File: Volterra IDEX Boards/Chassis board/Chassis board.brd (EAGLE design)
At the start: 102.2 x 54 mm, 28 parts, among them K1 FFC/FPC/34PIN/1MMPITCH/TOPLOCK, K2 FFC/FPC/34PIN/1MMPITCH/TOPLOCK, K3 FFC/FPC/34PIN/1MMPITCH/TOPLOCK

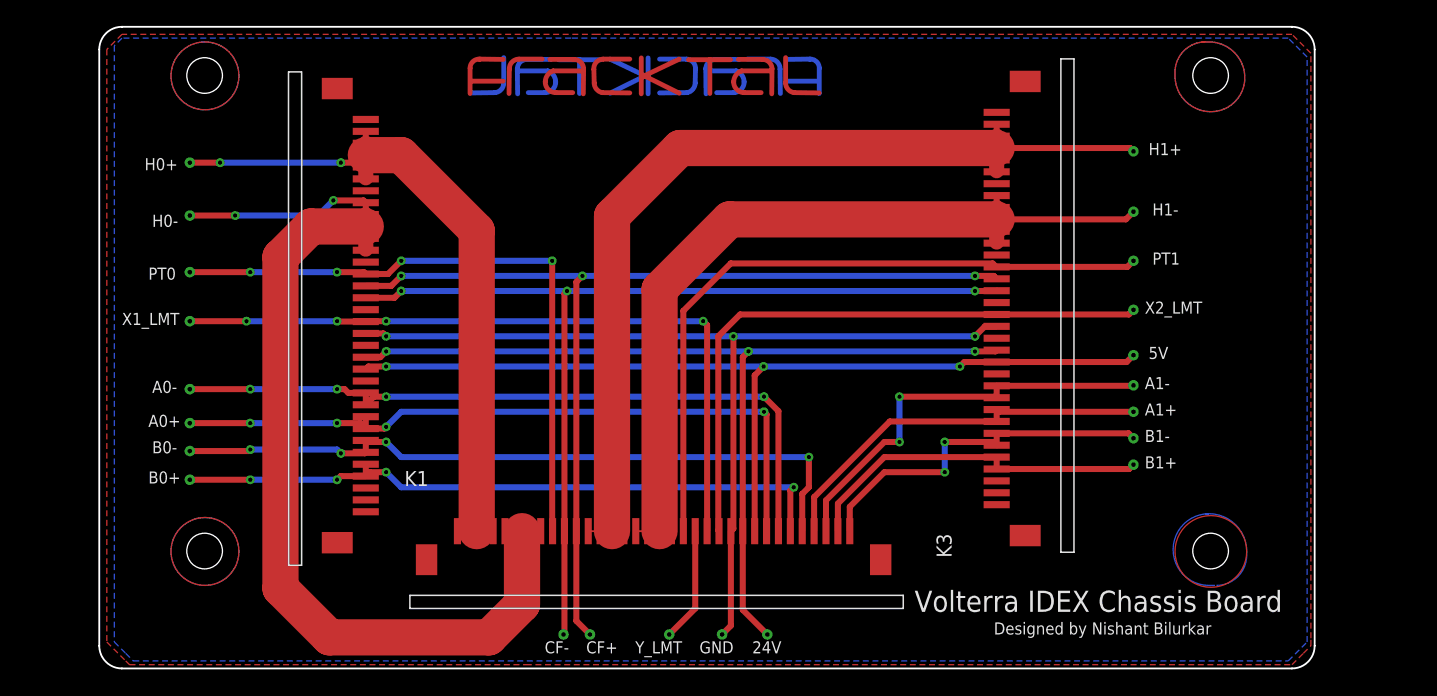
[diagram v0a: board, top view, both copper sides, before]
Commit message: Switching of carriage board numbering, changing extruder FFC pins and fixing routings
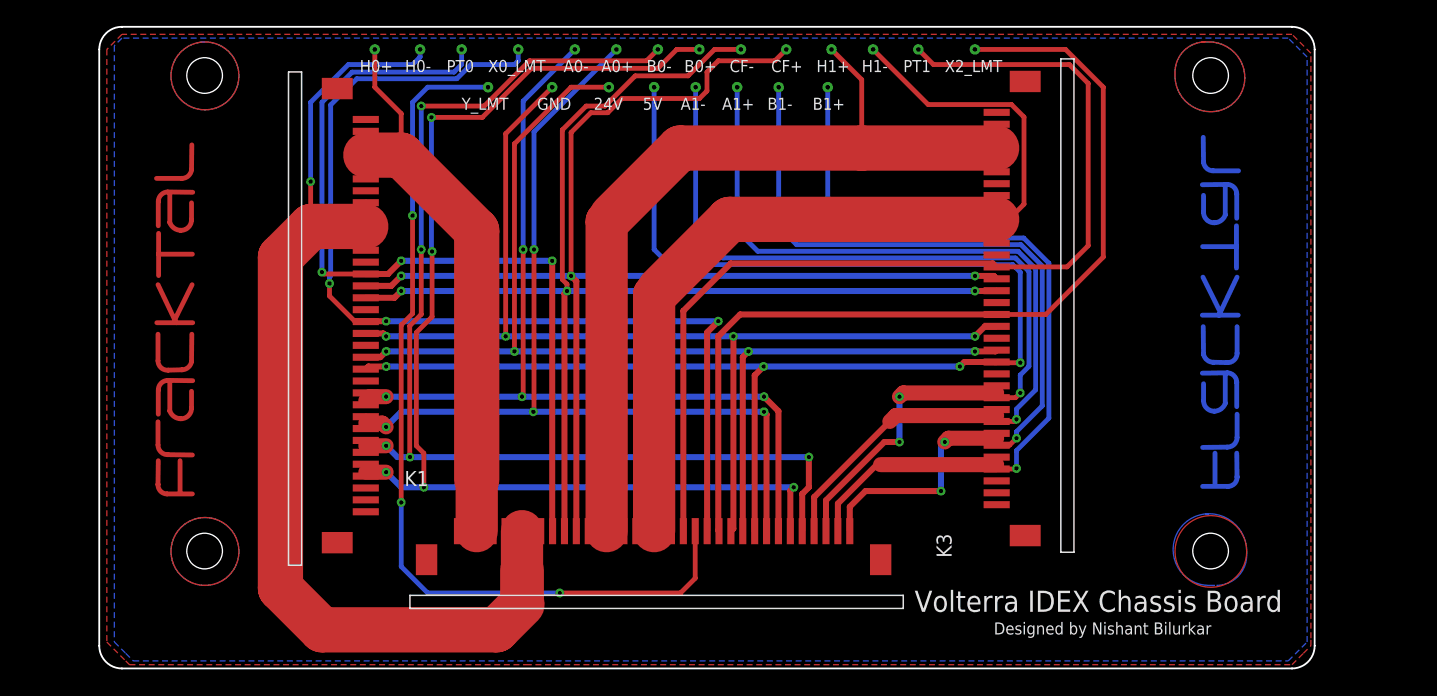
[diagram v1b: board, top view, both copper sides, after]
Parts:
- moved TP19 56.1 mm to (58.1, 55.9)
- moved TP3 51.9 mm to (65.4, 55.9)
- moved TP18 51.9 mm to (54.6, 55.9)
- moved TP4 51.4 mm to (61.6, 55.9)
- moved U$3 48.9 mm to (100.3, 31.1), turned to 90 degrees
- moved TP13 48.5 mm to (40.3, 52.7)
- moved TP6 48.2 mm to (45.7, 52.7)
- moved TP7 47.9 mm to (50.5, 52.7)
- moved TP20 47.7 mm to (51.1, 55.9)
- moved TP8 46.2 mm to (54.3, 52.7)
- moved TP14 44.6 mm to (57.8, 52.7)
- moved TP9 43.2 mm to (47.6, 55.9)
- moved TP15 43.1 mm to (61.3, 52.7)
- moved TP16 42.0 mm to (64.8, 52.7)
- moved U$2 41.3 mm to (15.6, 30.5), turned to 90 degrees
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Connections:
- removed net X2_LMT: K1.23, K3.17, TP12.P$1
- new net X0_LMT: K1.22, K2.18, TP5.P$1
- net X1_LMT: now also K1.23, K3.17, TP12.P$1; no longer K1.22, K2.18, TP5.P$1
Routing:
- net X0_LMT: track 0.00 -> 86.1 mm, vias 0 -> 3
- net Y_LMT: track 9.60 -> 76.4 mm, vias 0 -> 3
- net X2_LMT: track 52.3 -> 0.00 mm
- net 5V: track 79.2 -> 122.6 mm, vias 3 -> 4
- net A1-: track 35.4 -> 78.1 mm, vias 2 -> 3
- net A1+: track 33.4 -> 75.6 mm, vias 0 -> 1
- net B0+: track 56.4 -> 98.2 mm, vias 4 -> 5
- net B1-: track 30.9 -> 72.6 mm, vias 2 -> 3
- net B1+: track 30.0 -> 69.4 mm, vias 0 -> 1
- net B0-: track 60.4 -> 96.9 mm, vias 4 -> 5
- net PT1: track 58.4 -> 84.3 mm
- net CF+: track 84.4 -> 109.2 mm
- net CF-: track 82.3 -> 105.1 mm
- net A0+: track 60.2 -> 78.7 mm
- net 24V: track 78.2 -> 96.0 mm, vias 3 -> 4
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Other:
- board text added: "X0_LMT"
- board text removed: "X1_LMT"

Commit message: Updated Daughter board schematic and other boards
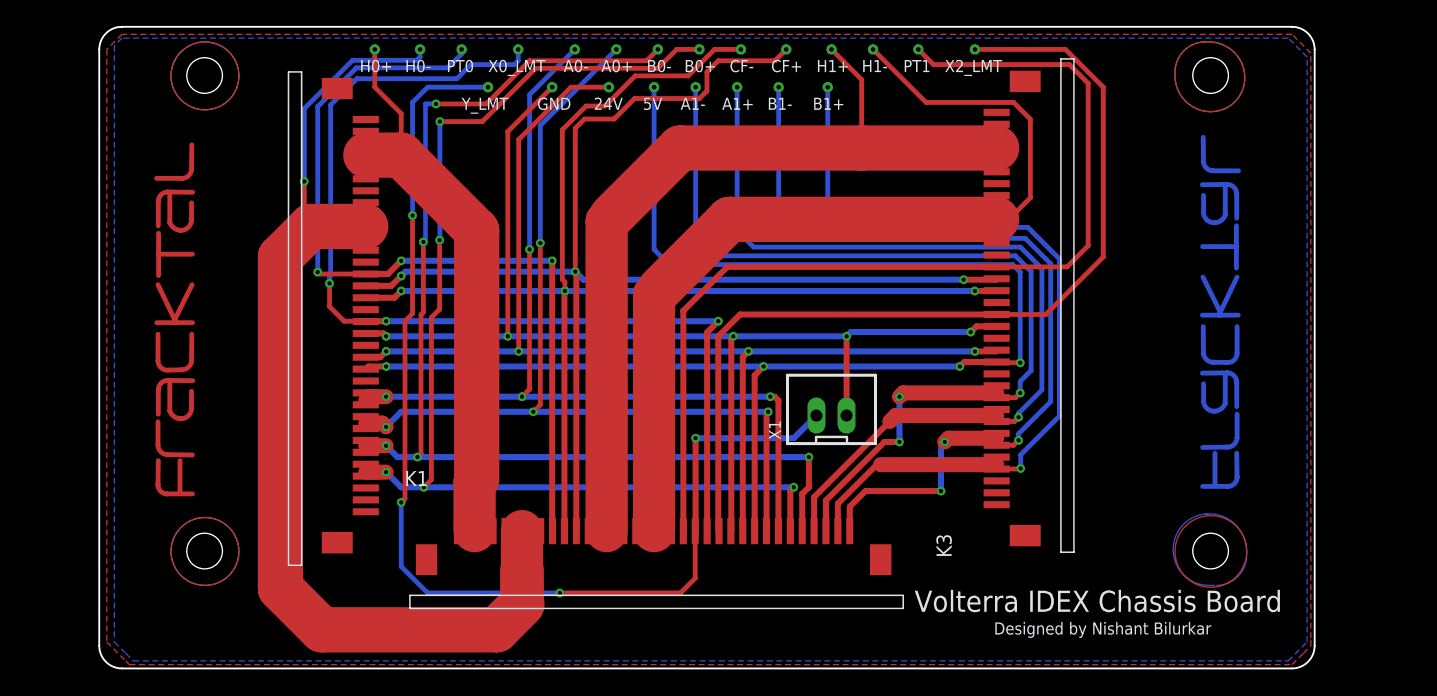
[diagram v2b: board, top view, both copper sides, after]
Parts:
- added X1: JST-XH-02-PIN-LONG-PAD, Rembrandt Electronics - JST XH Connectors v1-0:JST-XH-02-PACKAGE-LONG-PAD
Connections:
- net GND: now also X1.2
- net Y_LMT: now also X1.1
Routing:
- net Y_LMT: track 76.4 -> 95.7 mm, vias 3 -> 4
- net GND: track 92.6 -> 99.2 mm, vias 4 -> 5
- net B1+: track 69.4 -> 71.0 mm
- net B1-: track 72.6 -> 73.9 mm
- net B0+: track 98.2 -> 97.0 mm
- net A1+: track 75.6 -> 76.4 mm
- net H1-: track 83.5 -> 84.2 mm
- net X0_LMT: track 86.1 -> 86.6 mm
- net A0-: track 77.5 -> 78.0 mm

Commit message: DRC checked of Chassis, Carriage 1 & 2, and created CAM files
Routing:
- net H0+: track 53.9 -> 55.4 mm
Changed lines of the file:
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@@
 <contactref element="K2" pad="6"/>
 <contactref element="TP21" pad="P$1"/>
-<wire x1="37.7505" y1="15.3595" x2="38.7505" y2="15.3595" width="0.1524" layer="1"/>
-<wire x1="38.7505" y1="15.3595" x2="39.1922" y2="15.3595" width="0.1524" layer="1"/>
-<wire x1="39.37" y1="15.3595" x2="39.7505" y2="15.3595" width="0.1524" layer="1"/>
-<wire x1="39.7505" y1="15.3595" x2="40.7505" y2="15.3595" width="0.1524" layer="1"/>
-<wire x1="39.1922" y1="19.5072" x2="39.37" y2="19.685" width="3.556" layer="1"/>
-<wire x1="39.1922" y1="19.5072" x2="39.1922" y2="15.3595" width="3.556" layer="1"/>
-<wire x1="39.37" y1="19.685" x2="39.37" y2="40.64" width="3.81" layer="1"/>
+<wire x1="39.1922" y1="18.796" x2="39.37" y2="18.9738" width="3.556" layer="1"/>
+<wire x1="39.1922" y1="15.7151" x2="39.1922" y2="18.796" width="3.556" layer="1"/>
+<wire x1="39.37" y1="18.9738" x2="39.37" y2="40.64" width="3.81" layer="1"/>
 <wire x1="30.04" y1="46.99" x2="33.02" y2="46.99" width="3.81" layer="1"/>
 <wire x1="39.37" y1="40.64" x2="33.02" y2="46.99" width="3.81" layer="1"/>
@@
 <wire x1="30.04" y1="46.99" x2="30.04" y2="45.99" width="0.508" layer="1"/>
 <wire x1="30.04" y1="45.99" x2="30.04" y2="44.99" width="0.508" layer="1"/>
+<wire x1="40.7505" y1="15.3595" x2="39.7505" y2="15.3595" width="0.2032" layer="1"/>
+<wire x1="37.7505" y1="15.3595" x2="38.7505" y2="15.3595" width="0.2032" layer="1"/>
+<wire x1="38.7505" y1="15.3595" x2="39.7505" y2="15.3595" width="0.2032" layer="1"/>
+<wire x1="37.7505" y1="15.3595" x2="38.1061" y2="15.7151" width="0.2032" layer="1"/>
+<wire x1="38.1061" y1="15.7151" x2="39.1922" y2="15.7151" width="0.2032" layer="1"/>
 </signal>
 <signal name="H0-">
@@
 <contactref element="K2" pad="11"/>
 <contactref element="TP1" pad="P$1"/>
-<wire x1="41.7505" y1="15.3595" x2="42.7505" y2="15.3595" width="0.1524" layer="1"/>
-<wire x1="43.7505" y1="15.3595" x2="43.18" y2="15.3595" width="0.1524" layer="1"/>
-<wire x1="42.7505" y1="15.3595" x2="43.18" y2="15.3595" width="0.1524" layer="1"/>
-<wire x1="43.7505" y1="15.3595" x2="44.7505" y2="15.3595" width="0.1524" layer="1"/>
-<wire x1="43.18" y1="15.3595" x2="43.18" y2="12.065" width="3.556" layer="1"/>
+<wire x1="43.18" y1="12.065" x2="43.18" y2="15.1817" width="3.556" layer="1"/>
 <wire x1="43.18" y1="12.065" x2="43.18" y2="9.2075" width="3.683" layer="1"/>
 <wire x1="43.18" y1="9.2075" x2="41.0337" y2="7.0612" width="3.81" layer="1"/>
@@
 <wire x1="30.04" y1="40.99" x2="30.04" y2="39.99" width="1.27" layer="1"/>
 <wire x1="30.04" y1="41.99" x2="30.04" y2="42.99" width="0.508" layer="1"/>
-<wire x1="30.04" y1="39.99" x2="30.04" y2="38.99" width="0.1524" layer="1"/>
 <wire x1="25.4325" y1="40.99" x2="24.8666" y2="41.5559" width="0.4064" layer="1"/>
 <wire x1="24.8666" y1="41.5559" x2="24.8666" y2="44.7675" width="0.4064" layer="1"/>
@@
 <wire x1="34.3281" y1="54.9656" x2="34.6075" y2="55.245" width="0.4064" layer="16"/>
 <wire x1="34.6075" y1="55.245" x2="34.6075" y2="55.88" width="0.4064" layer="16"/>
+<wire x1="41.7505" y1="15.3595" x2="42.7505" y2="15.3595" width="0.2032" layer="1"/>
+<wire x1="42.7505" y1="15.3595" x2="43.7505" y2="15.3595" width="0.2032" layer="1"/>
+<wire x1="43.7505" y1="15.3595" x2="44.7505" y2="15.3595" width="0.2032" layer="1"/>
+<wire x1="43.18" y1="15.1817" x2="43.3578" y2="15.3595" width="0.2032" layer="1"/>
+<wire x1="43.3578" y1="15.3595" x2="43.7505" y2="15.3595" width="0.2032" layer="1"/>
+<wire x1="30.04" y1="39.99" x2="30.04" y2="38.99" width="0.2032" layer="1"/>
 </signal>
 <signal name="PT0">
@@
 <contactref element="K3" pad="29"/>
 <contactref element="TP22" pad="P$1"/>
-<wire x1="48.7505" y1="15.3595" x2="49.7505" y2="15.3595" width="0.1524" layer="1"/>
-<wire x1="49.7505" y1="15.3595" x2="50.2984" y2="15.3595" width="0.1524" layer="1"/>
-<wire x1="50.2984" y1="15.3595" x2="50.7505" y2="15.3595" width="0.1524" layer="1"/>
-<wire x1="50.7505" y1="15.3595" x2="51.7505" y2="15.3595" width="0.1524" layer="1"/>
 <wire x1="83.107" y1="47.587" x2="71.755" y2="47.587" width="3.81" layer="1"/>
 <wire x1="71.755" y1="47.587" x2="56.477" y2="47.587" width="3.81" layer="1"/>
@@
 <wire x1="83.107" y1="47.587" x2="83.107" y2="46.587" width="1.27" layer="1"/>
 <wire x1="83.107" y1="48.587" x2="83.107" y2="49.587" width="0.508" layer="1"/>
-<wire x1="83.107" y1="46.587" x2="83.107" y2="45.587" width="0.1524" layer="1"/>
 <wire x1="69.215" y1="55.88" x2="71.755" y2="53.34" width="0.4064" layer="1"/>
 <wire x1="71.755" y1="53.34" x2="71.755" y2="47.587" width="0.4064" layer="1"/>
 <wire x1="50.7505" y1="41.8605" x2="50.2984" y2="41.4084" width="3.556" layer="1"/>
-<wire x1="50.2984" y1="41.4084" x2="50.2984" y2="15.3595" width="3.556" layer="1"/>
+<wire x1="50.2984" y1="41.4084" x2="50.2984" y2="15.7151" width="3.556" layer="1"/>
+<wire x1="48.7505" y1="15.3595" x2="49.7505" y2="15.3595" width="0.2032" layer="1"/>
+<wire x1="50.7505" y1="15.3595" x2="51.7505" y2="15.3595" width="0.2032" layer="1"/>
+<wire x1="50.7505" y1="15.3595" x2="49.7505" y2="15.3595" width="0.2032" layer="1"/>
+<wire x1="50.2984" y1="15.7151" x2="50.654" y2="15.3595" width="0.2032" layer="1"/>
+<wire x1="50.654" y1="15.3595" x2="50.7505" y2="15.3595" width="0.2032" layer="1"/>
+<wire x1="83.107" y1="46.587" x2="83.107" y2="45.587" width="0.2032" layer="1"/>
 </signal>
 <signal name="H1-">
@@
 <contactref element="K3" pad="23"/>
 <contactref element="TP10" pad="P$1"/>
-<wire x1="52.7505" y1="15.3595" x2="53.7505" y2="15.3595" width="0.1524" layer="1"/>
-<wire x1="53.7505" y1="15.3595" x2="54.2925" y2="15.3595" width="0.1524" layer="1"/>
-<wire x1="54.2925" y1="15.3595" x2="54.7505" y2="15.3595" width="0.1524" layer="1"/>
-<wire x1="54.7505" y1="15.3595" x2="55.7505" y2="15.3595" width="0.1524" layer="1"/>
 <wire x1="60.637" y1="41.587" x2="83.107" y2="41.587" width="3.81" layer="1"/>
 <wire x1="60.637" y1="41.587" x2="54.7505" y2="35.7005" width="3.81" layer="1"/>
-<wire x1="83.107" y1="39.587" x2="83.107" y2="40.587" width="0.1524" layer="1"/>
-<wire x1="83.107" y1="40.587" x2="83.107" y2="41.587" width="0.1524" layer="1"/>
-<wire x1="83.107" y1="41.587" x2="83.107" y2="42.587" width="0.1524" layer="1"/>
-<wire x1="83.107" y1="42.587" x2="83.107" y2="43.587" width="0.1524" layer="1"/>
 <wire x1="54.7505" y1="35.7005" x2="54.2925" y2="35.2425" width="3.556" layer="1"/>
-<wire x1="54.2925" y1="35.2425" x2="54.2925" y2="15.3595" width="3.556" layer="1"/>
+<wire x1="54.2925" y1="35.2425" x2="54.2925" y2="15.5373" width="3.556" layer="1"/>
 <wire x1="72.7075" y1="55.88" x2="77.1671" y2="51.4204" width="0.4064" layer="1"/>
 <wire x1="77.1671" y1="51.4204" x2="84.53209375" y2="51.4204" width="0.4064" layer="1"/>
@@
 <wire x1="85.9409" y1="43.3959" x2="84.132" y2="41.587" width="0.4064" layer="1"/>
 <wire x1="84.132" y1="41.587" x2="83.107" y2="41.587" width="0.4064" layer="1"/>
+<wire x1="52.7505" y1="15.3595" x2="53.7505" y2="15.3595" width="0.2032" layer="1"/>
+<wire x1="53.7505" y1="15.3595" x2="54.7505" y2="15.3595" width="0.2032" layer="1"/>
+<wire x1="55.7505" y1="15.3595" x2="54.7505" y2="15.3595" width="0.2032" layer="1"/>
+<wire x1="54.2925" y1="15.5373" x2="54.4703" y2="15.3595" width="0.2032" layer="1"/>
+<wire x1="54.4703" y1="15.3595" x2="54.7505" y2="15.3595" width="0.2032" layer="1"/>
+<wire x1="83.107" y1="43.587" x2="83.107" y2="42.587" width="0.2032" layer="1"/>
+<wire x1="83.107" y1="42.587" x2="83.107" y2="41.587" width="0.2032" layer="1"/>
+<wire x1="83.107" y1="41.587" x2="83.107" y2="40.587" width="0.2032" layer="1"/>
+<wire x1="83.107" y1="40.587" x2="83.107" y2="39.587" width="0.2032" layer="1"/>
 </signal>
 <signal name="PT1">
@@
 <contactref element="K3" pad="10"/>
 <contactref element="TP14" pad="P$1"/>
-<wire x1="83.107" y1="26.67" x2="83.107" y2="26.587" width="0.1524" layer="1"/>
 <wire x1="68.7505" y1="15.3595" x2="68.7505" y2="17.9505" width="0.508" layer="1"/>
 <wire x1="73.66" y1="22.86" x2="68.7505" y2="17.9505" width="0.508" layer="1"/>
@@
 <wire x1="84.6895" y1="26.587" x2="83.107" y2="26.587" width="0.4064" layer="1"/>
 <wire x1="57.785" y1="40.64" x2="59.9059" y2="38.5191" width="0.4064" layer="16"/>
-<wire x1="83.107" y1="27.587" x2="83.107" y2="26.9875" width="0.4064" layer="1"/>
-<wire x1="83.107" y1="26.9875" x2="83.107" y2="26.67" width="0.4064" layer="1"/>
-<wire x1="83.107" y1="26.9875" x2="75.2475" y2="26.9875" width="1.27" layer="1"/>
-<wire x1="75.2475" y1="26.9875" x2="74.93" y2="26.67" width="1.27" layer="1"/>
+<wire x1="74.93" y1="26.67" x2="75.2475" y2="26.9875" width="1.27" layer="1"/>
+<wire x1="83.107" y1="27.587" x2="83.107" y2="27.0256" width="0.2032" layer="1"/>
+<wire x1="83.107" y1="27.0256" x2="83.107" y2="26.587" width="0.2032" layer="1"/>
+<wire x1="83.0689" y1="26.9875" x2="83.107" y2="27.0256" width="1.27" layer="1"/>
+<wire x1="75.2475" y1="26.9875" x2="83.0689" y2="26.9875" width="1.27" layer="1"/>
 </signal>
 <signal name="B1+">

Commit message: Board files added
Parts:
- flipped TP1 to the bottom
- flipped TP10 to the bottom
- flipped TP11 to the bottom
- flipped TP12 to the bottom
- flipped TP13 to the bottom
- flipped TP14 to the bottom
- flipped TP15 to the bottom
- flipped TP16 to the bottom
- flipped TP17 to the bottom
- flipped TP18 to the bottom
- flipped TP19 to the bottom
- flipped TP2 to the bottom
- flipped TP20 to the bottom
- flipped TP21 to the bottom
- flipped TP22 to the bottom
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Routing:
- net B1-: track 73.9 -> 75.5 mm, vias 3 -> 4
- net A1-: track 78.4 -> 77.6 mm, vias 3 -> 4
- net A0+: track 79.0 -> 79.7 mm, vias 4 -> 7
- net B0-: track 96.6 -> 97.1 mm, vias 5 -> 6
- net B1+: track 71.0 -> 70.7 mm, vias 1 -> 2
- net PT0: track 71.2 -> 71.0 mm, vias 3 -> 4
- net X0_LMT: track 86.6 -> 86.4 mm, vias 3 -> 4
- net H0-: track 94.7 -> 94.5 mm, vias 1 -> 2
- net A1+: track 76.4 -> 76.6 mm, vias 1 -> 2
- net Y_LMT: track 95.7 -> 95.6 mm, vias 4 -> 5
- net H1+: vias 0 -> 1
- net GND: vias 5 -> 6
- net 5V: vias 4 -> 5
- net H0+: vias 0 -> 1
- net X1_LMT: vias 0 -> 1
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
